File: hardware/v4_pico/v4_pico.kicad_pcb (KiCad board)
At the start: 2 copper layers, 92.3 x 96 mm, 110 parts, among them J1 joystick, J10 ON/OFF, J11 MIDI IN bk: 5 R: 4, J2 LED strip, J3 SSD1306 SPI, J4 MIDI OUT Y:M5 - R:M4, J5 Batt, J6 Neck - Y:O BK:B R:3.3, J7 01x03, J8 MXP5010, J9 Thumb, Q1 2N7000, SW1 SW_DIP_x01, U1 74HC165, U2 74HC165, U3 74HC165, U4 Pico, U5 FJ08K, U6 6N138, U7 MCP3002

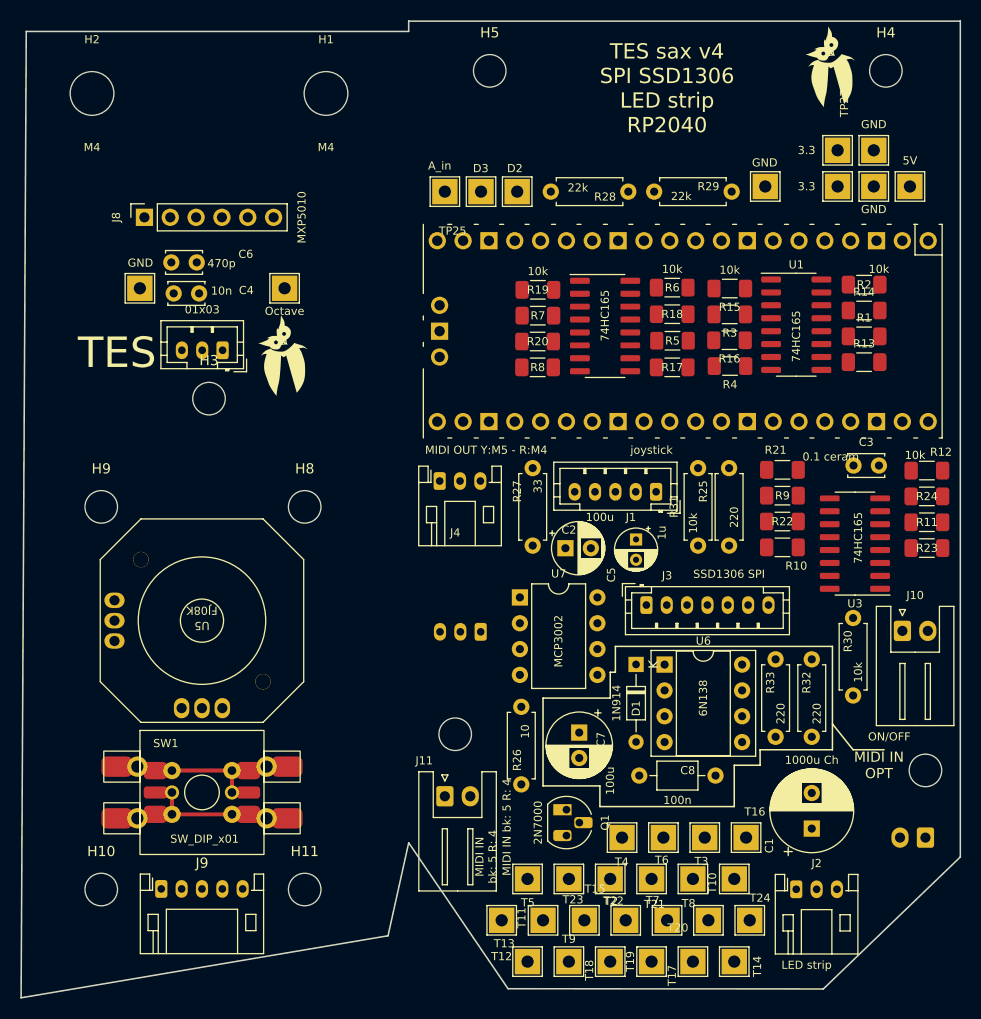
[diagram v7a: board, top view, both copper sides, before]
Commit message: PCB cured and routed
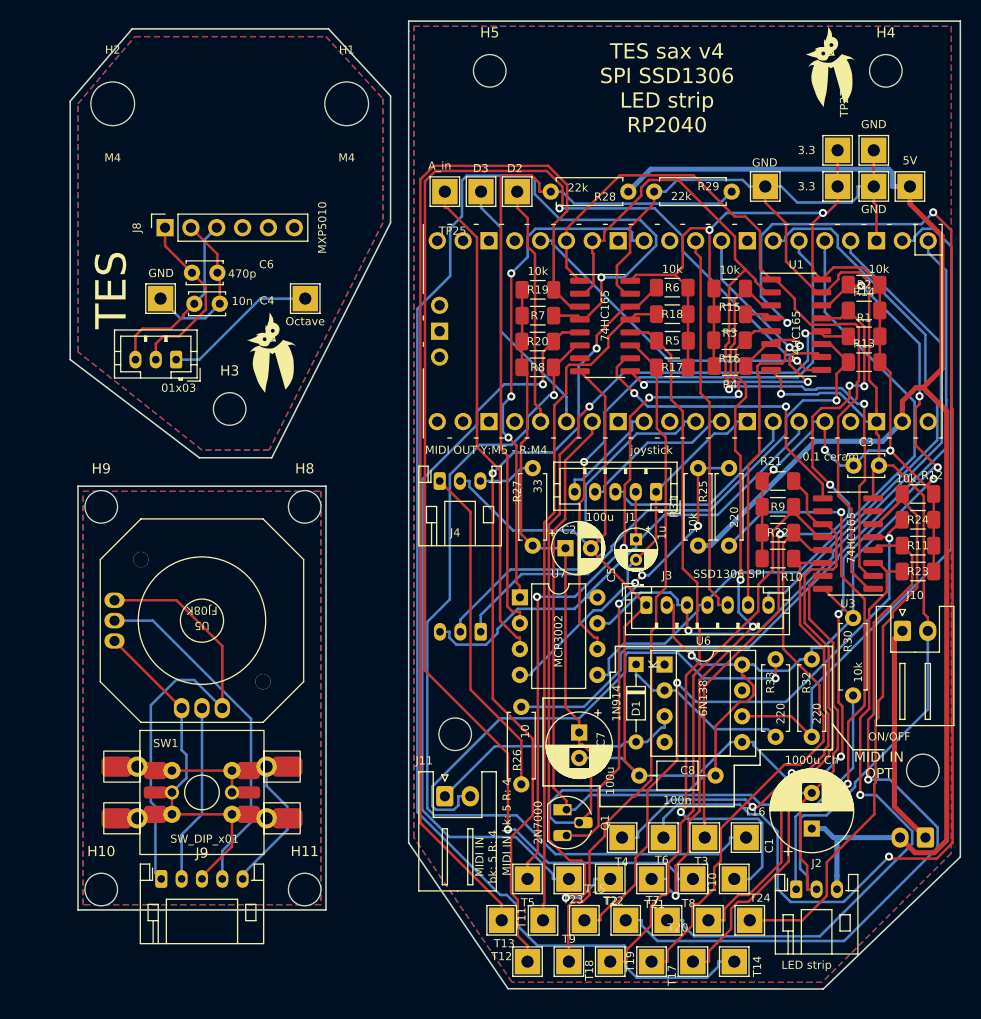
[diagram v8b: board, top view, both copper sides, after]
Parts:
- moved J7 4.66 mm to (179.7, 49.8)
- moved R11 2.46 mm to (252.6, 68.1)
- moved R12 2.46 mm to (252.6, 63.0)
- moved R23 2.46 mm to (252.6, 70.6)
- moved R24 2.46 mm to (252.6, 65.5)
- moved J8 2.27 mm to (178.6, 36.8)
- moved C4 2.27 mm to (184.0, 44.3)
- moved C6 2.27 mm to (183.8, 41.2)
- moved TP37 2.27 mm to (178.2, 43.8)
- moved H1 2.27 mm to (196.5, 24.6)
- moved H2 2.27 mm to (173.5, 24.6)
- moved H3 2.27 mm to (185.0, 54.6)
- moved TP36 2.27 mm to (192.4, 43.8)
- moved R22 1.19 mm to (238.9, 66.8)
- moved R21 1.19 mm to (238.9, 61.7)
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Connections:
- C5 pad 2: GND -> GNDA
- J9 pad 1: Net-(J9-Pad1) -> Net-(U5-Pad4)
- J9 pad 3: Net-(J9-Pad3) -> Net-(SW1-Pad2)
- SW1 pad 2: Net-(J9-Pad1) -> Net-(SW1-Pad2)
- U5 pad 1: Net-(J9-Pad3) -> Net-(SW1-Pad2)
- U5 pad 3: Net-(J9-Pad1) -> Net-(U5-Pad4)
- U5 pad 4: Net-(J9-Pad3) -> Net-(U5-Pad4)
- U5 pad 6: Net-(J9-Pad1) -> Net-(SW1-Pad2)
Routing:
- net GND: track 0.00 -> 276.1 mm, vias 0 -> 1
- net +3.3V: track 0.00 -> 267.0 mm, vias 0 -> 7
- net +5V: track 0.00 -> 146.9 mm
- net Net-(R7-Pad1): track 0.00 -> 143.3 mm, vias 0 -> 1
- net Net-(R4-Pad1): track 0.00 -> 142.0 mm, vias 0 -> 3
- net Net-(R3-Pad1): track 0.00 -> 135.5 mm, vias 0 -> 3
- net Net-(R19-Pad1): track 0.00 -> 106.0 mm
- net Net-(R1-Pad1): track 0.00 -> 89.8 mm, vias 0 -> 3
- net Net-(R8-Pad1): track 0.00 -> 88.3 mm, vias 0 -> 1
- net Net-(R2-Pad1): track 0.00 -> 84.7 mm, vias 0 -> 7
- net Net-(R6-Pad1): track 0.00 -> 79.1 mm, vias 0 -> 2
- net Net-(Q1-Pad1): track 0.00 -> 78.0 mm
- net /SR_CLK: track 0.00 -> 78.0 mm, vias 0 -> 2
- net Net-(R15-Pad1): track 0.00 -> 78.0 mm, vias 0 -> 4
- net Net-(R11-Pad1): track 0.00 -> 74.6 mm, vias 0 -> 1
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- added copper zone on B.Cu, net GND
- added copper zone on F.Cu, net GND
- added copper zone on B.Cu, net Net-(C4-Pad1)
- added copper zone on F.Cu, net Net-(C4-Pad1)
- added copper zone on B.Cu, net Net-(U5-Pad4)
- added copper zone on F.Cu, net Net-(U5-Pad4)
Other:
- board size 92.3 x 96 mm -> 87.5 x 95.1 mm
